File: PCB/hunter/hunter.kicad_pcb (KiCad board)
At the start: 2 copper layers, 36.2 x 52.6 mm, 0 parts

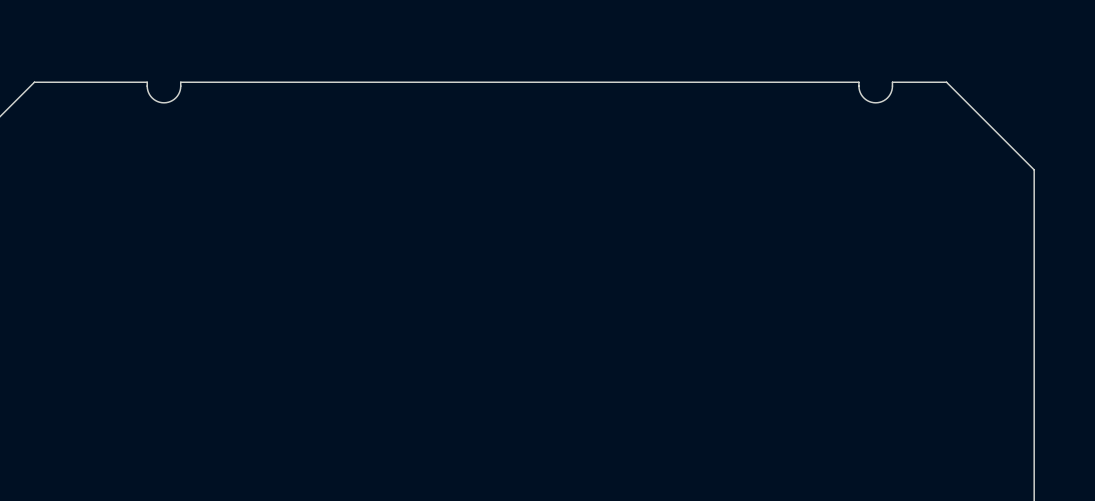
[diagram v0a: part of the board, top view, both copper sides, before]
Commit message: first button, correction to the board cut
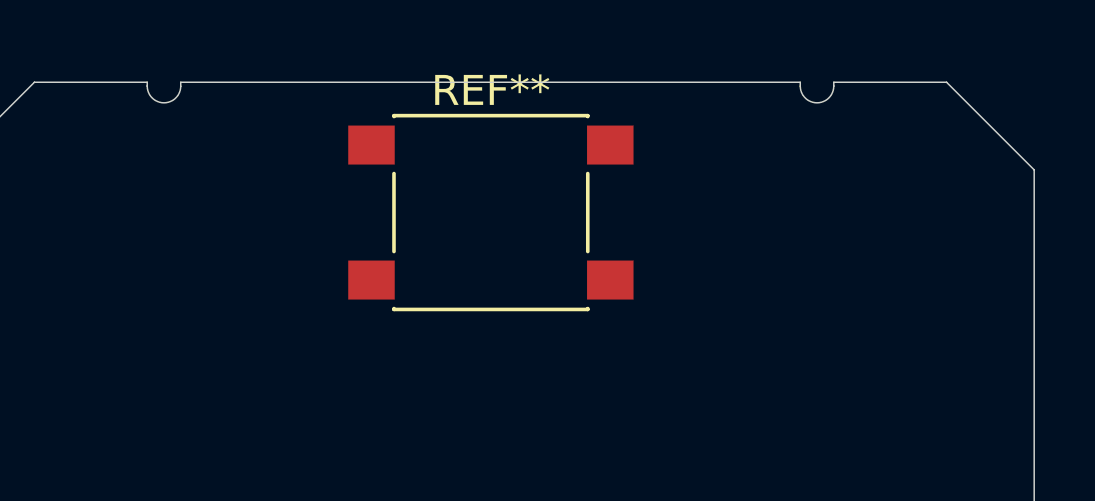
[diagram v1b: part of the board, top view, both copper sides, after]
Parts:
- added REF**: SW_SPST_PTS645, Button_Switch_SMD:SW_SPST_PTS645, F.Cu at (68.2, 54.4)
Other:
- outline, holes or cut-outs redrawn
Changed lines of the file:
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@@
     (tracks 0)
     (zones 0)
-    (modules 0)
+    (modules 1)
     (nets 1)
   )
@@
     (uvia_drill 0.1)
   )
+  (module Button_Switch_SMD:SW_SPST_PTS645 (layer F.Cu)
+    (at 68.1736 54.3814)
+    (descr "C&K Components SPST SMD PTS645 Series 6mm Tact Switch")
+    (tags "SPST Button Switch")
+    (attr smd)
+    (fp_text reference REF** (at 0 -4.05) (layer F.SilkS)
+      (effects (font (size 1 1) (thickness 0.15)))
+    )
+    (fp_text value SW_SPST_PTS645 (at 0 4.15) (layer F.Fab)
+      (effects (font (size 1 1) (thickness 0.15)))
+    )
+    (fp_circle (center 0 0) (end 1.75 -0.05) (layer F.Fab) (width 0.1))
+    (fp_line (start -3.23 3.23) (end 3.23 3.23) (layer F.SilkS) (width 0.12))
+    (fp_line (start -3.23 -1.3) (end -3.23 1.3) (layer F.SilkS) (width 0.12))
+    (fp_line (start -3.23 -3.23) (end 3.23 -3.23) (layer F.SilkS) (width 0.12))
+    (fp_line (start 3.23 -1.3) (end 3.23 1.3) (layer F.SilkS) (width 0.12))
+    (fp_line (start -3.23 -3.2) (end -3.23 -3.23) (layer F.SilkS) (width 0.12))
+    (fp_line (start -3.23 3.23) (end -3.23 3.2) (layer F.SilkS) (width 0.12))
+    (fp_line (start 3.23 3.23) (end 3.23 3.2) (layer F.SilkS) (width 0.12))
+    (fp_line (start 3.23 -3.23) (end 3.23 -3.2) (layer F.SilkS) (width 0.12))
+    (fp_line (start -5.05 -3.4) (end 5.05 -3.4) (layer F.CrtYd) (width 0.05))
+    (fp_line (start -5.05 3.4) (end 5.05 3.4) (layer F.CrtYd) (width 0.05))
+    (fp_line (start -5.05 -3.4) (end -5.05 3.4) (layer F.CrtYd) (width 0.05))
+    (fp_line (start 5.05 3.4) (end 5.05 -3.4) (layer F.CrtYd) (width 0.05))
+    (fp_line (start 3 -3) (end -3 -3) (layer F.Fab) (width 0.1))
+    (fp_line (start 3 3) (end 3 -3) (layer F.Fab) (width 0.1))
+    (fp_line (start -3 3) (end 3 3) (layer F.Fab) (width 0.1))
+    (fp_line (start -3 -3) (end -3 3) (layer F.Fab) (width 0.1))
+    (fp_text user %R (at 0 -4.05) (layer F.Fab)
+      (effects (font (size 1 1) (thickness 0.15)))
+    )
+    (pad 2 smd rect (at 3.98 2.25) (size 1.55 1.3) (layers F.Cu F.Paste F.Mask))
+    (pad 1 smd rect (at 3.98 -2.25) (size 1.55 1.3) (layers F.Cu F.Paste F.Mask))
+    (pad 1 smd rect (at -3.98 -2.25) (size 1.55 1.3) (layers F.Cu F.Paste F.Mask))
+    (pad 2 smd rect (at -3.98 2.25) (size 1.55 1.3) (layers F.Cu F.Paste F.Mask))
+    (model ${KISYS3DMOD}/Button_Switch_SMD.3dshapes/SW_SPST_PTS645.wrl
+      (at (xyz 0 0 0))
+      (scale (xyz 1 1 1))
+      (rotate (xyz 0 0 0))
+    )
+  )
   (gr_circle (center 81.28 83.6676) (end 82.1182 83.6676) (layer Edge.Cuts) (width 0.05))
   (gr_circle (center 55.0418 83.6676) (end 55.88 83.6676) (layer Edge.Cuts) (width 0.05))
@@
   (gr_arc (start 50.038 95.631) (end 50.038 96.2914) (angle -180) (layer Edge.Cuts) (width 0.05))
   (gr_line (start 50.038 102.6668) (end 50.038 96.2914) (layer Edge.Cuts) (width 0.05))
-  (gr_arc (start 81.0006 50.165) (end 80.4418 50.165) (angle -180) (layer Edge.Cuts) (width 0.05))
-  (gr_line (start 81.5594 50.038) (end 83.3628 50.038) (layer Edge.Cuts) (width 0.05))
-  (gr_line (start 80.4418 50.165) (end 80.4418 50.038) (layer Edge.Cuts) (width 0.05))
-  (gr_line (start 81.5594 50.165) (end 81.5594 50.038) (layer Edge.Cuts) (width 0.05))
+  (gr_arc (start 79.0448 50.165) (end 78.486 50.165) (angle -180) (layer Edge.Cuts) (width 0.05))
+  (gr_line (start 79.6036 50.038) (end 83.3628 50.038) (layer Edge.Cuts) (width 0.05))
+  (gr_line (start 78.486 50.165) (end 78.486 50.038) (layer Edge.Cuts) (width 0.05))
+  (gr_line (start 79.6036 50.165) (end 79.6036 50.038) (layer Edge.Cuts) (width 0.05))
   (gr_line (start 57.8358 50.165) (end 57.8358 50.038) (layer Edge.Cuts) (width 0.05))
   (gr_line (start 56.7182 50.165) (end 56.7182 50.038) (layer Edge.Cuts) (width 0.05))
   (gr_arc (start 57.277 50.165) (end 56.7182 50.165) (angle -180) (layer Edge.Cuts) (width 0.05))
-  (gr_line (start 57.8358 50.038) (end 80.4418 50.038) (layer Edge.Cuts) (width 0.05))
+  (gr_line (start 57.8358 50.038) (end 78.486 50.038) (layer Edge.Cuts) (width 0.05))
   (gr_line (start 64.66831 102.641308) (end 64.6684 102.6668) (layer Edge.Cuts) (width 0.05))
   (gr_arc (start 68.173601 106.146599) (end 71.7042 102.6668) (angle -90.41517954) (layer Edge.Cuts) (width 0.05))

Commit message: Fully functional PCB (Phase 2) (#8)
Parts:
- removed REF**: SW_SPST_PTS645, Button_Switch_SMD:SW_SPST_PTS645
- added AE1: Antenna, Connector_PinHeader_2.54mm:PinHeader_1x01_P2.54mm_Vertical, F.Cu at (52.0, 75.1)
- added C101: 27pF, Capacitor_SMD:C_0402_1005Metric, F.Cu at (52.2, 53.4)
- added C121: 6.8pF, Capacitor_SMD:C_0402_1005Metric, F.Cu at (53.4, 69.2)
- added C122: 12pF, Capacitor_SMD:C_0402_1005Metric, F.Cu at (51.6, 71.8)
- added C123: 6.8pF, Capacitor_SMD:C_0402_1005Metric, F.Cu at (53.0, 72.8)
- added C124: 220pF, Capacitor_SMD:C_0402_1005Metric, F.Cu at (52.0, 68.6)
- added C125: 220pF, Capacitor_SMD:C_0402_1005Metric, F.Cu at (54.4, 73.2)
- added C131: 6.8pF, Capacitor_SMD:C_0402_1005Metric, F.Cu at (54.8, 67.6)
- added C51: 100nF, Capacitor_SMD:C_0402_1005Metric, F.Cu at (59.6, 57.0)
- added C61: 10uF, Capacitor_Tantalum_SMD:CP_EIA-3216-18_Kemet-A, F.Cu at (76.4, 56.2)
- added C81: 27pF, Capacitor_SMD:C_0402_1005Metric, F.Cu at (57.7, 53.4)
- added D11: LED1, LED_SMD:LED_0603_1608Metric, F.Cu at (61.0, 73.6)
- added D2: LED2, LED_SMD:LED_0603_1608Metric, F.Cu at (75.7, 73.6)
- added H1: MountingHole, MountingHole:MountingHole_2mm, F.Cu at (55.0, 83.7)
- added H2: MountingHole, MountingHole:MountingHole_2mm, F.Cu at (81.2, 83.6)
- added J1: Battery, parts:MyBatteryConnector, F.Cu at (62.8, 97.9)
- added J2: JTAG, Connector_PinHeader_2.54mm:PinHeader_1x04_P2.54mm_Vertical, F.Cu at (81.1, 65.0)
- added L121: 33nH, Inductor_SMD:L_0402_1005Metric, F.Cu at (52.8, 67.6)
- added L122: 18nH, Inductor_SMD:L_0402_1005Metric, F.Cu at (53.0, 71.2)
- added L123: 33nH, Inductor_SMD:L_0402_1005Metric, F.Cu at (54.4, 71.2)
- added L131: 33nH, Inductor_SMD:L_0402_1005Metric, F.Cu at (54.4, 69.2)
- added R171: 56k, Resistor_SMD:R_0402_1005Metric, F.Cu at (55.2, 62.0)
- added SW1: SW_Light, Button_Switch_SMD:SW_SPST_Omron_B3FS-100xP, F.Cu at (68.1, 54.4)
- added SW2: SW_LightUp, Button_Switch_SMD:SW_SPST_Omron_B3FS-100xP, F.Cu at (61.0, 66.6)
- added SW3: SW_LightDown, Button_Switch_SMD:SW_SPST_Omron_B3FS-100xP, F.Cu at (75.6, 66.6)
- added SW4: SW_Fan, Button_Switch_SMD:SW_SPST_Omron_B3FS-100xP, F.Cu at (68.1, 80.4)
- added SW5: SW_FanUp, Button_Switch_SMD:SW_SPST_Omron_B3FS-100xP, F.Cu at (60.6, 92.7)
- added SW6: SW_FanDown, Button_Switch_SMD:SW_SPST_Omron_B3FS-100xP, F.Cu at (75.7, 92.7)
- added U1: RGP20_2P4X2P4, parts:CC1101RGPR, F.Cu at (55.8, 58.0)
- added U2: UFQFPN20_3x3x0p6, parts:STM8L101F3U6TR, F.Cu at (68.2, 66.0)
- added Y1: 25MHz, Crystal:Crystal_SMD_3225-4Pin_3.2x2.5mm, F.Cu at (54.8, 52.8)
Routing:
- net Net-(AE1-Pad1): track 0.00 -> 147.1 mm
- net +3V0: track 0.00 -> 116.6 mm, vias 0 -> 5
- net GND: track 0.00 -> 84.3 mm, vias 0 -> 15
- net Net-(D2-Pad2): track 0.00 -> 46.6 mm
- net Net-(SW5-Pad2): track 0.00 -> 24.5 mm
- net Net-(SW6-Pad1): track 0.00 -> 24.3 mm
- net Net-(U1-Pad6): track 0.00 -> 20.4 mm, vias 0 -> 2
- net Net-(U1-Pad7): track 0.00 -> 20.1 mm
- net Net-(J2-Pad4): track 0.00 -> 19.2 mm
- net Net-(U1-Pad2): track 0.00 -> 16.1 mm, vias 0 -> 2
- net Net-(C121-Pad1): track 0.00 -> 14.8 mm
- net Net-(D11-Pad2): track 0.00 -> 14.7 mm, vias 0 -> 2
- net Net-(C131-Pad2): track 0.00 -> 14.1 mm
- net Net-(U1-Pad20): track 0.00 -> 13.5 mm
- net Net-(U1-Pad1): track 0.00 -> 12.9 mm
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- added copper zone on B.Cu, net GND
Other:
- outline, holes or cut-outs redrawn
